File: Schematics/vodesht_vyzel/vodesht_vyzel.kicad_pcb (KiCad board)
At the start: 2 copper layers, 3 parts, among them U1 SSD1306, U2 NODEMCU32S, U3 NRF52840-DONGLE

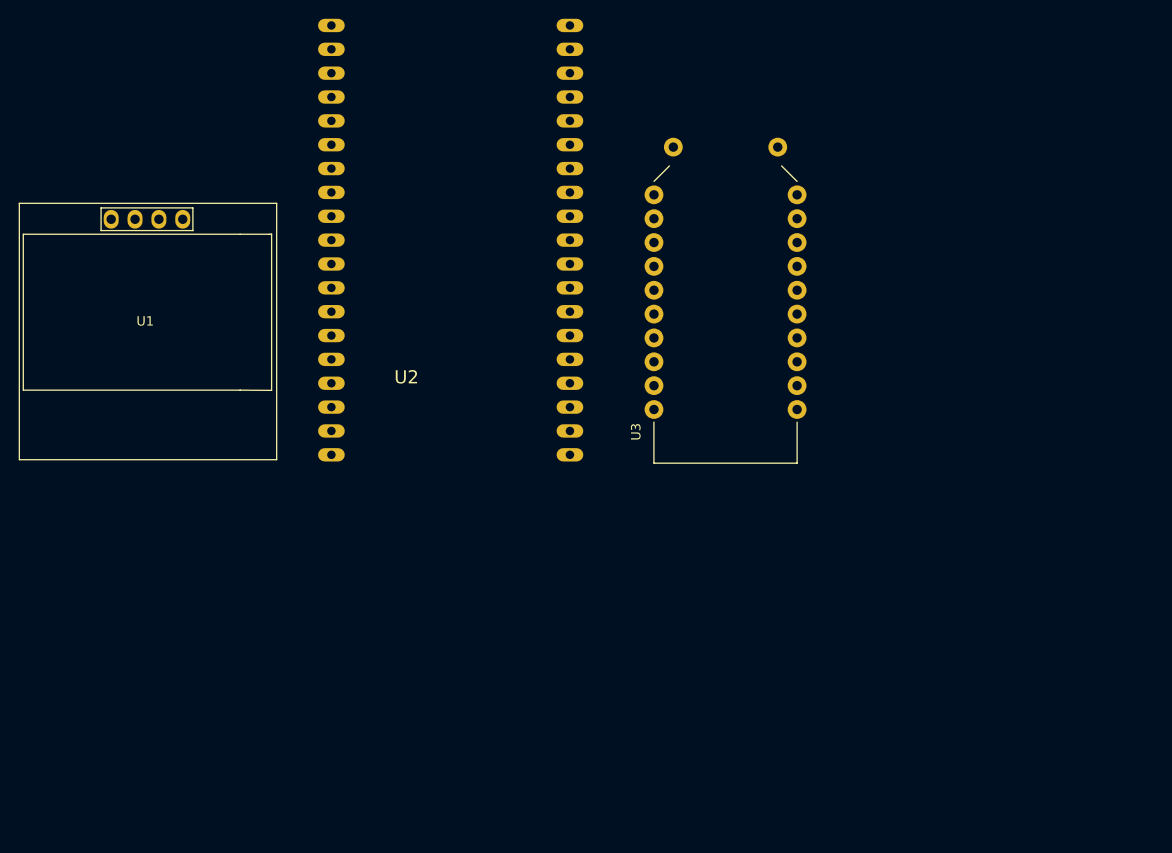
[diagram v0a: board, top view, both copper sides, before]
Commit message: Edited the pcb board of the vodesht_vyzel and did some small changes on the pcb of the main module
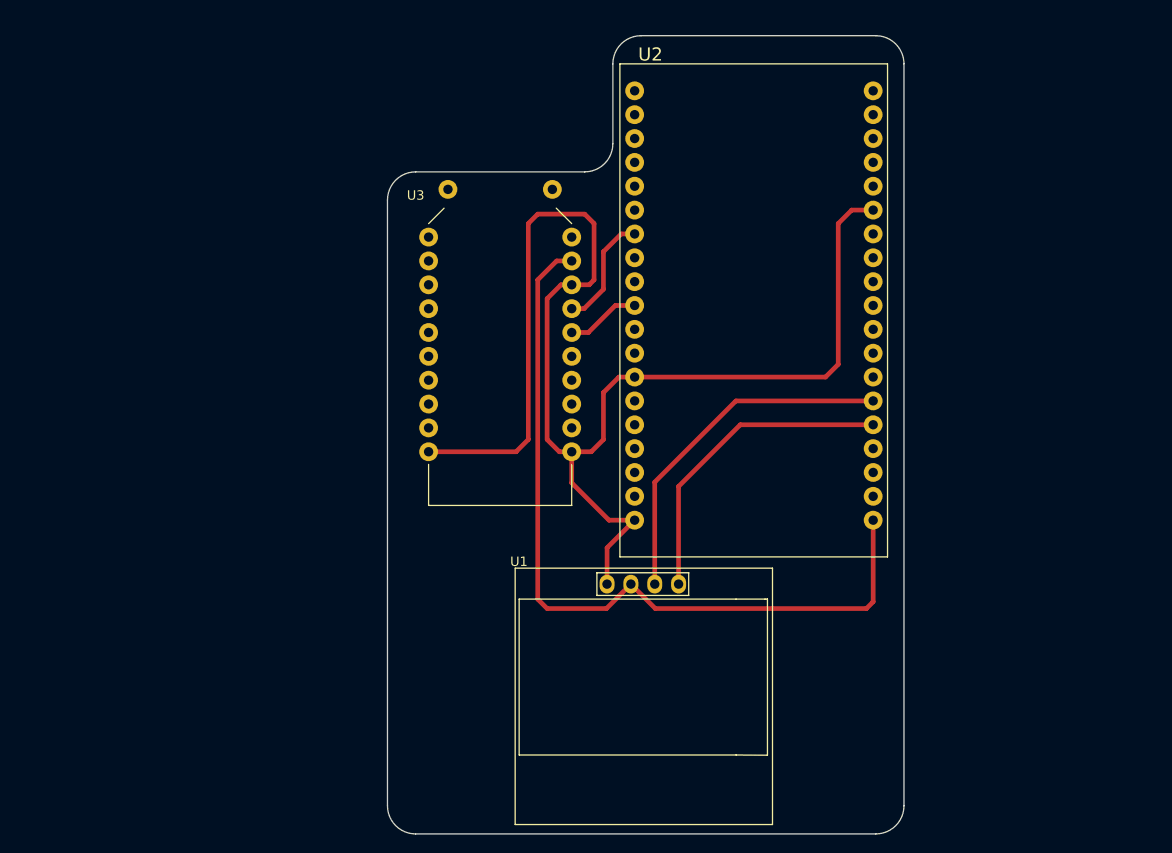
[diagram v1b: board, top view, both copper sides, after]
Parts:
- moved U1 65.6 mm to (142.0, 129.0)
- moved U2 31.2 mm to (152.8, 90.0), turned to 180 degrees
- moved U3 24.4 mm to (127.0, 87.0)
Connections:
- U2 pad 3V3: (no net) -> +3.3V
- U3 pad 0.20: Net-(U2-PadP4) -> unconnected-(U3-Pad0.20)
- U3 pad 0.24: Net-(U2-PadP5) -> unconnected-(U3-Pad0.24)
- U3 pad 0.29: unconnected-(U3-Pad0.29) -> Net-(U2-PadP5)
- U3 pad 0.31: unconnected-(U3-Pad0.31) -> Net-(U2-PadP4)
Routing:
- net GNDD: track 0.00 -> 146.1 mm
- net +3.3V: track 0.00 -> 85.7 mm
- net Net-(U1-Pad3): track 0.00 -> 37.7 mm
- net Net-(U1-Pad4): track 0.00 -> 33.8 mm
- net Net-(U2-PadP4): track 0.00 -> 12.3 mm
- net Net-(U2-PadP5): track 0.00 -> 7.89 mm
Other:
- board outline added: 55 x 85 mm

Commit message: Fixed some footprints and made changes on the leader node pcb
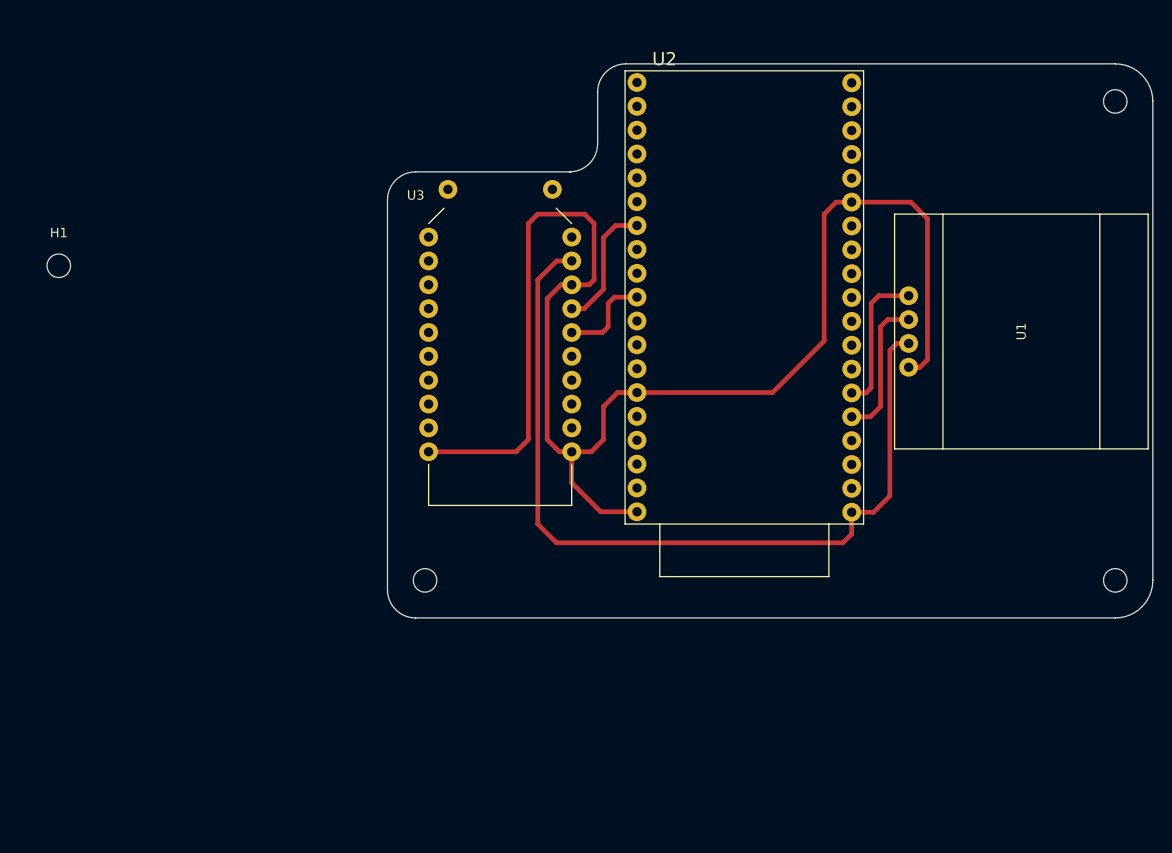
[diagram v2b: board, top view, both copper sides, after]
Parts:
- added H1: MountingHole, MountingHole:MountingHole_2.5mm, F.Cu at (80.0, 84.5)
- added H2: MountingHole, MountingHole:MountingHole_2.5mm, F.Cu at (192.5, 67.0)
- added H3: MountingHole, MountingHole:MountingHole_2.5mm, F.Cu at (119.0, 118.0)
- added H4: MountingHole, MountingHole:MountingHole_2.5mm, F.Cu at (192.5, 118.0)
- moved U1 55.2 mm to (182.5, 91.5), turned to 90 degrees
- moved U2 4.51 mm to (153.0, 85.5)
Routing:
- net Net-(U1-Pad3): track 37.7 -> 15.3 mm
- net Net-(U1-Pad4): track 33.8 -> 15.6 mm
- net GNDD: track 146.1 -> 160.4 mm
- net Net-(U2-Pad32): track 0.00 -> 13.8 mm
- net Net-(U2-PadP4): track 12.3 -> 0.00 mm
- net Net-(U2-Pad29): track 0.00 -> 9.97 mm
- net Net-(U2-PadP5): track 7.89 -> 0.00 mm
- net +3.3V: track 85.7 -> 90.0 mm
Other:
- board size 55 x 85 mm -> 81.5 x 59 mm

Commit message: Made small changes in the schematics
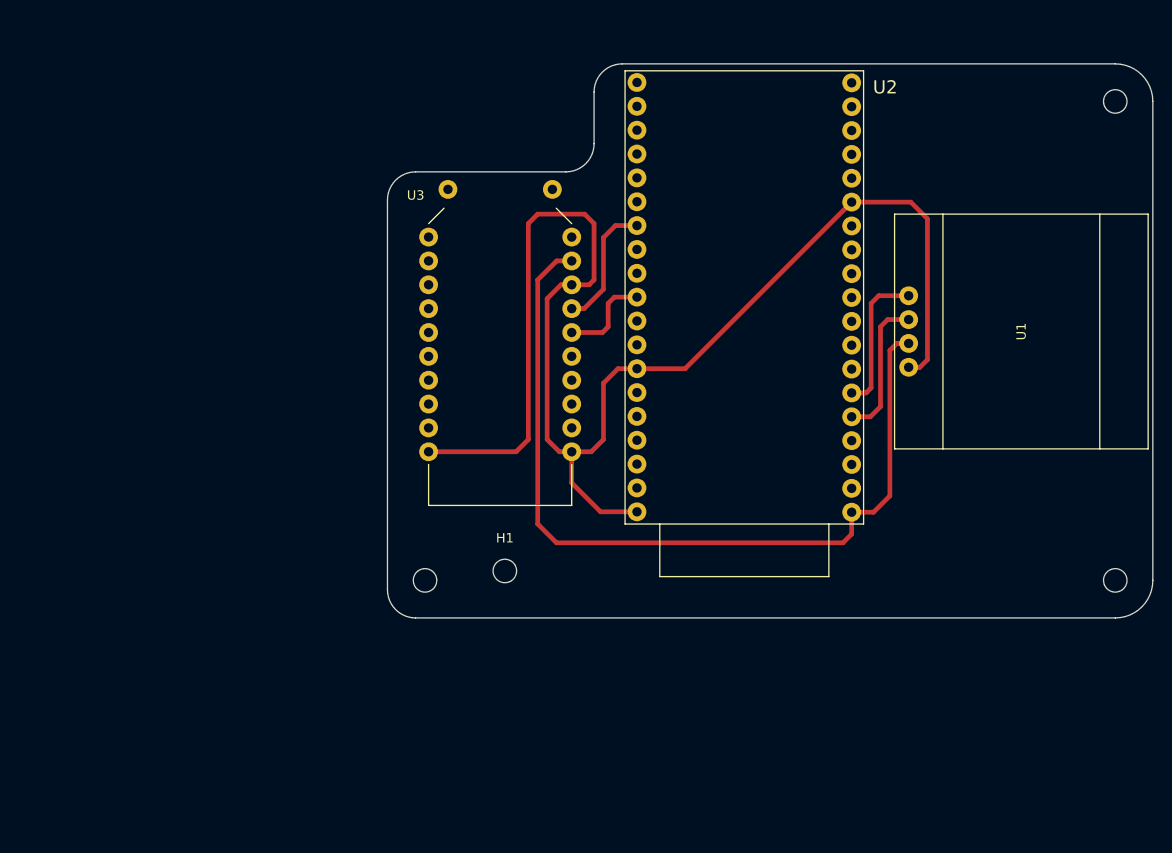
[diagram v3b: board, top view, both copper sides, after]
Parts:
- moved H1 57.6 mm to (127.5, 117.0)
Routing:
- net GNDD: track 160.4 -> 154.0 mm
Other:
- outline, holes or cut-outs redrawn
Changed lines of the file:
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@@
   )
   (footprint "MountingHole:MountingHole_2.5mm" (layer "F.Cu")
-    (at 80 84.5)
+    (at 127.5 117)
     (descr "Mounting Hole 2.5mm, no annular")
     (tags "mounting hole 2.5mm no annular")
@@
     (property "Sheetname" "")
     (attr through_hole)
-    (fp_text reference "U2" (at 8.5 23) (layer "F.SilkS")
+    (fp_text reference "U2" (at -15 20) (layer "F.SilkS")
       (effects (font (size 1.4 1.4) (thickness 0.15)))
     )
@@
       (net 52 "unconnected-(U2-Pad38)") (pinfunction "CLK") (pintype "bidirectional+no_connect"))
     (model "C:/Diplomna/3Dmodels/esp32-wroom-32s-nodemcu-32s-1.snapshot.8/ESP32Wroom32s.STEP"
-      (offset (xyz 915.5 -120.5 -471.5))
+      (offset (xyz -915 125 -471.5))
       (scale (xyz 1 1 1))
-      (rotate (xyz -90 0 90))
+      (rotate (xyz -90 0 -90))
     )
   )
@@
   )
   (gr_line (start 196.5 118) (end 196.5 67) (layer "Edge.Cuts") (width 0.1))
-  (gr_line (start 137.37868 66) (end 137.37868 71.5) (layer "Edge.Cuts") (width 0.1))
-  (gr_line (start 192.5 63) (end 140.37868 63) (layer "Edge.Cuts") (width 0.1))
-  (gr_arc (start 137.37868 66) (mid 138.25736 63.87868) (end 140.37868 63) (layer "Edge.Cuts") (width 0.1))
-  (gr_line (start 118 74.5) (end 134.5 74.5) (layer "Edge.Cuts") (width 0.1))
-  (gr_arc (start 118 122) (mid 115.87868 121.12132) (end 115 119) (layer "Edge.Cuts") (width 0.1))
+  (gr_line (start 137 66) (end 137 71.5) (layer "Edge.Cuts") (width 0.1))
+  (gr_arc (start 137 66) (mid 137.87868 63.87868) (end 140 63) (layer "Edge.Cuts") (width 0.1))
+  (gr_line (start 192.5 63) (end 140 63) (layer "Edge.Cuts") (width 0.1))
+  (gr_line (start 118 74.5) (end 134 74.5) (layer "Edge.Cuts") (width 0.1))
   (gr_arc (start 192.5 63) (mid 195.328427 64.171573) (end 196.5 67) (layer "Edge.Cuts") (width 0.1))
   (gr_arc (start 196.5 118) (mid 195.328427 120.828427) (end 192.5 122) (layer "Edge.Cuts") (width 0.1))
   (gr_arc (start 115 77.5) (mid 115.87868 75.37868) (end 118 74.5) (layer "Edge.Cuts") (width 0.1))
-  (gr_arc (start 137.37868 71.5) (mid 136.5 73.62132) (end 134.37868 74.5) (layer "Edge.Cuts") (width 0.1))
+  (gr_arc (start 137 71.5) (mid 136.12132 73.62132) (end 134 74.5) (layer "Edge.Cuts") (width 0.1))
+  (gr_arc (start 118 122) (mid 115.87868 121.12132) (end 115 119) (layer "Edge.Cuts") (width 0.1))
   (gr_line (start 115 77.5) (end 115 119) (layer "Edge.Cuts") (width 0.1))
   (gr_line (start 118 122) (end 192.5 122) (layer "Edge.Cuts") (width 0.1))
   (segment (start 131 79) (end 136 79) (width 0.5) (layer "F.Cu") (net 1))
   (segment (start 134.62 107.62) (end 137.7 110.7) (width 0.5) (layer "F.Cu") (net 1))
-  (segment (start 156 98) (end 161.5 92.5) (width 0.5) (layer "F.Cu") (net 1))
   (segment (start 171.69 95.31) (end 170.5 95.31) (width 0.5) (layer "F.Cu") (net 1))
-  (segment (start 141.57 98) (end 156 98) (width 0.5) (layer "F.Cu") (net 1))
   (segment (start 137 80) (end 137 86) (width 0.5) (layer "F.Cu") (net 1))
-  (segment (start 136.695 104.305) (end 138 103) (width 0.5) (layer "F.Cu") (net 1))
   (segment (start 134.62 104.305) (end 133.305 104.305) (width 0.5) (layer "F.Cu") (net 1))
   (segment (start 128.695 104.305) (end 130 103) (width 0.5) (layer "F.Cu") (net 1))
+  (segment (start 141.57 95.46) (end 139.54 95.46) (width 0.5) (layer "F.Cu") (net 1))
   (segment (start 133.305 104.305) (end 132 103) (width 0.5) (layer "F.Cu") (net 1))
+  (segment (start 138 97) (end 138 103) (width 0.5) (layer "F.Cu") (net 1))
   (segment (start 170.72 77.72) (end 172.5 79.5) (width 0.5) (layer "F.Cu") (net 1))
+  (segment (start 146.69 95.46) (end 164.43 77.72) (width 0.5) (layer "F.Cu") (net 1))
   (segment (start 137 86) (end 136.475 86.525) (width 0.5) (layer "F.Cu") (net 1))
   (segment (start 172.5 94.5) (end 171.69 95.31) (width 0.5) (layer "F.Cu") (net 1))
   (segment (start 134.62 107.62) (end 134.62 104.305) (width 0.5) (layer "F.Cu") (net 1))
-  (segment (start 138 103) (end 138 99.5) (width 0.5) (layer "F.Cu") (net 1))
+  (segment (start 141.57 95.46) (end 146.69 95.46) (width 0.5) (layer "F.Cu") (net 1))
   (segment (start 132 103) (end 132 88) (width 0.5) (layer "F.Cu") (net 1))
   (segment (start 119.38 104.305) (end 128.695 104.305) (width 0.5) (layer "F.Cu") (net 1))
   (segment (start 164.43 77.72) (end 170.72 77.72) (width 0.5) (layer "F.Cu") (net 1))
-  (segment (start 138 99.5) (end 139.5 98) (width 0.5) (layer "F.Cu") (net 1))
-  (segment (start 134.62 104.305) (end 136.695 104.305) (width 0.5) (layer "F.Cu") (net 1))
   (segment (start 136 79) (end 137 80) (width 0.5) (layer "F.Cu") (net 1))
   (segment (start 130 103) (end 130 80) (width 0.5) (layer "F.Cu") (net 1))
   (segment (start 130 80) (end 131 79) (width 0.5) (layer "F.Cu") (net 1))
-  (segment (start 139.5 98) (end 141.57 98) (width 0.5) (layer "F.Cu") (net 1))
-  (segment (start 161.5 79) (end 162.78 77.72) (width 0.5) (layer "F.Cu") (net 1))
-  (segment (start 161.5 92.5) (end 161.5 79) (width 0.5) (layer "F.Cu") (net 1))
   (segment (start 136.475 86.525) (end 134.62 86.525) (width 0.5) (layer "F.Cu") (net 1))
   (segment (start 133.475 86.525) (end 134.62 86.525) (width 0.5) (layer "F.Cu") (net 1))
-  (segment (start 162.78 77.72) (end 164.43 77.72) (width 0.5) (layer "F.Cu") (net 1))
+  (segment (start 136.695 104.305) (end 134.62 104.305) (width 0.5) (layer "F.Cu") (net 1))
+  (segment (start 139.54 95.46) (end 138 97) (width 0.5) (layer "F.Cu") (net 1))
+  (segment (start 138 103) (end 136.695 104.305) (width 0.5) (layer "F.Cu") (net 1))
   (segment (start 132 88) (end 133.475 86.525) (width 0.5) (layer "F.Cu") (net 1))
   (segment (start 172.5 79.5) (end 172.5 94.5) (width 0.5) (layer "F.Cu") (net 1))

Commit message: Changes on the vodesht_vyzel pcb and schematics
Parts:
- removed H4: MountingHole, MountingHole:MountingHole_2.5mm
- added G***: LOGO, LOGO, F.Cu at (132.5, 75.5)
- moved H2 92.4 mm to (119.0, 123.0), turned to 180 degrees
- moved H3 86.3 mm to (192.0, 72.0), turned to 180 degrees
- moved U3 59.7 mm to (184.5, 103.0), turned to -90 degrees
- moved U1 54.0 mm to (129.0, 98.5), turned to -90 degrees
- moved H1 45.8 mm to (119.0, 72.0)
- moved U2 19.8 mm to (158.5, 104.5), turned to 0 degrees
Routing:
- net GNDD: track 154.0 -> 162.2 mm
- net Net-(U2-Pad32): track 13.8 -> 14.4 mm
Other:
- board size 81.5 x 59 mm -> 81 x 59 mm
- board text added: "Lyubomir Nachev"
- board text added: "PCB v1.0"
